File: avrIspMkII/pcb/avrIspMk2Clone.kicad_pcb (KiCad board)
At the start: 2 copper layers, 50 x 40 mm, 42 parts, among them IC1 ATMEGA8-16AU, J1 DB9, P1 USB_OTG, P2 CONN_01X03, P3 CONN_01X02, P4 CONN_02X05, P5 CONN_02X03, SW1 SW_SPDT, SW2 SW_SPDT, U1 LM1117-3.3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

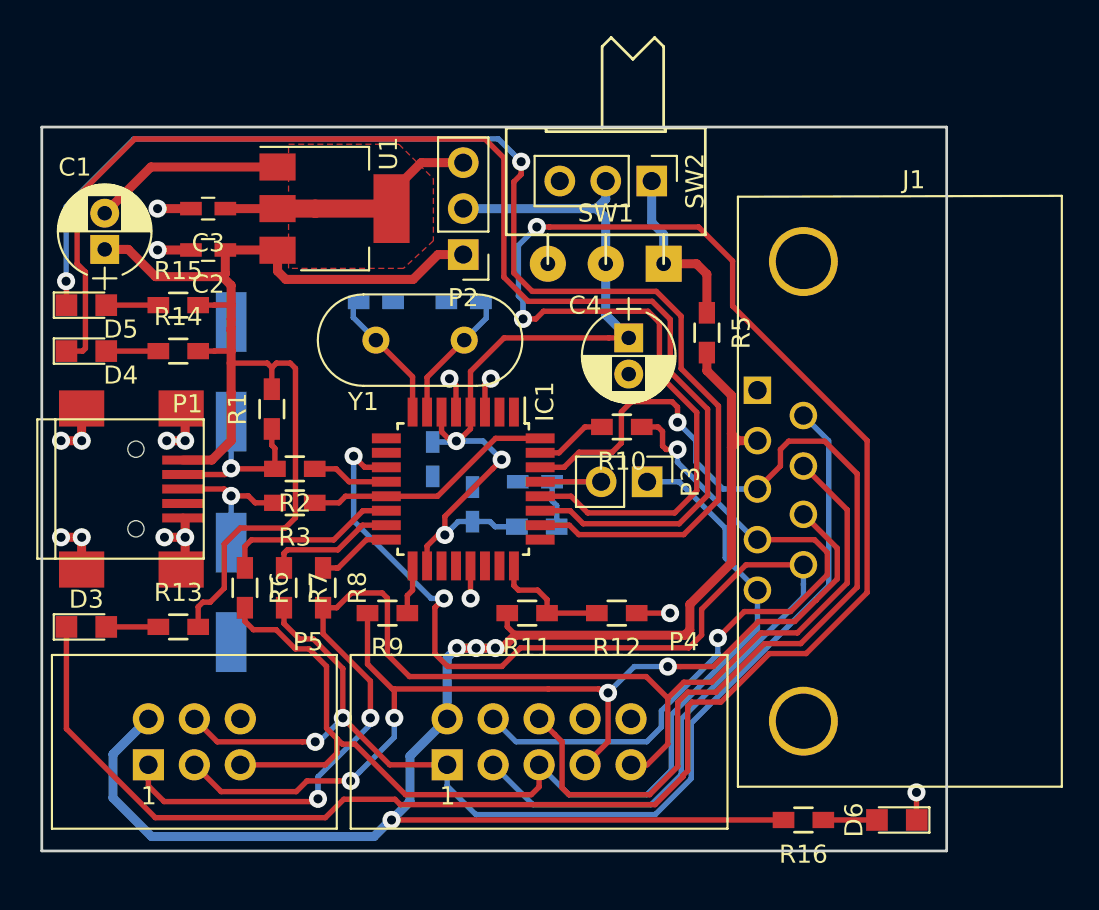
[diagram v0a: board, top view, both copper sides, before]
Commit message: finished layout for avrIspMk2Clone
generated documentation and gerber files
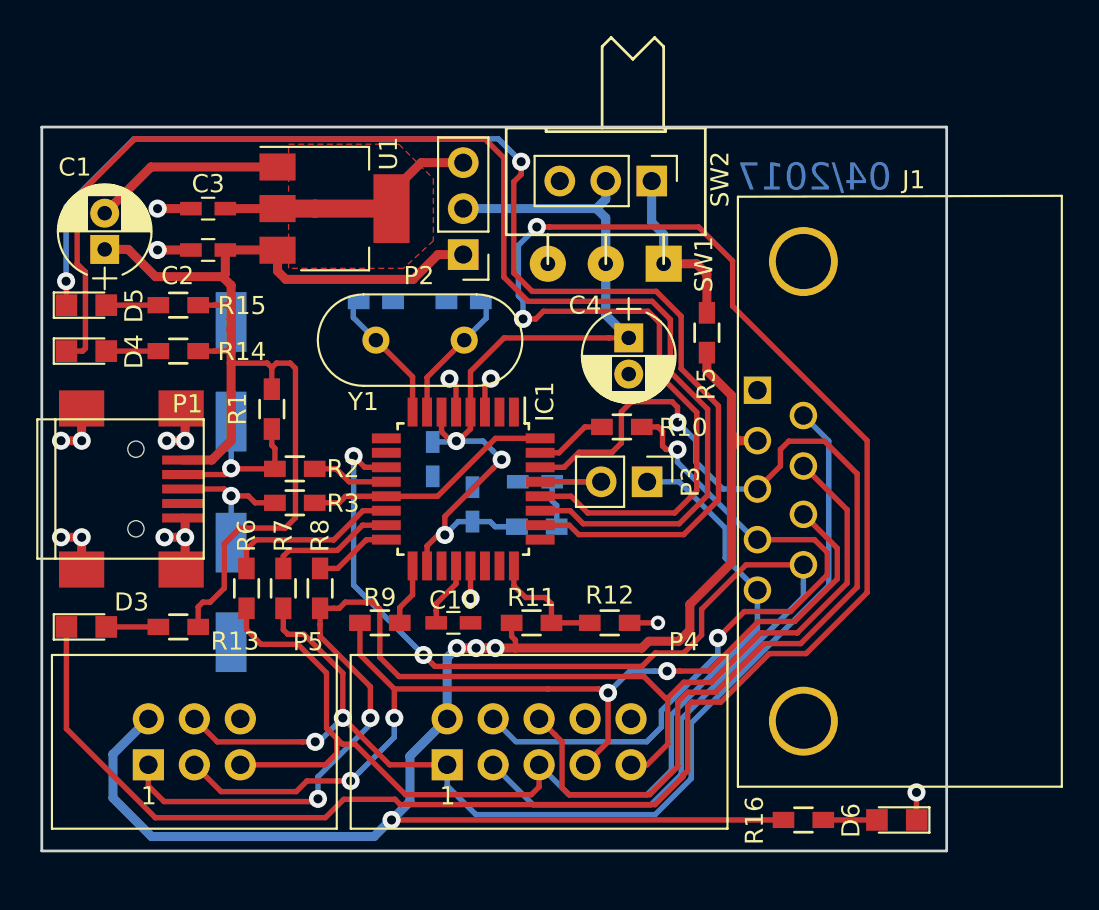
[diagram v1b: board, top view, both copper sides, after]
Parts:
- added C10: 100n, Capacitors_SMD:C_0603_HandSoldering, F.Cu at (102.7, 112.4)
- added G***: LOGO, proz_logo:Shimatta_SolderMask, B.Cu at (126.5, 105.0)
- added REF**: KiCAD Logo, Symbols:Symbol_KiCAD-Logo_CopperAndSilkScreenTop, B.Cu at (94.4, 89.4)
- added REF***: WEEE-Logo_4.2x6mm_SilkScreen, Symbols:WEEE-Logo_4.2x6mm_SilkScreen, B.Cu at (84.8, 112.1)
- moved R9 0.68 mm to (98.7, 112.4)
- moved R12 0.67 mm to (111.4, 112.4)
- moved R11 0.59 mm to (107.1, 112.4)
- moved R8 0.17 mm to (95.4, 110.5)
- moved R6 0.09 mm to (91.3, 110.5)
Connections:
- net /MEASSURE renamed /MEASURE
- IC1 pad 20: (no net) -> /AVREF
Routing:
- net /AVREF: track 0.00 -> 3.60 mm
- net Net-(IC1-Pad17): track 2.79 -> 3.44 mm
- net /MISO_OUT: track 72.6 -> 72.0 mm
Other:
- board text added: "04/2017"

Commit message: finished some layouts
added pcb numbering and revision
added a pcb list
orderes the pcbs
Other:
- board text added: "05/2017 Rev: 1.0 0001"
- board text removed: "04/2017"
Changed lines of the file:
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@@
-(kicad_pcb (version 20160815) (host pcbnew "(2017-01-09 revision c2fb336)-makepkg")
+(kicad_pcb (version 20170123) (host pcbnew "(2017-05-12 revision b823d0b78)-makepkg")
   (general
-    (links 0)
+    (links 102)
     (no_connects 0)
-    (area 79.924999 84.924999 130.075001 125.075001)
+    (area 71.380048 79.728999 145.469001 126.6055)
     (thickness 1.6)
     (drawings 5)
@@
   )
   (page A4)
+  (title_block
+    (title avrIspMk2Clone)
+    (date 2017-05-13)
+    (rev 1.0)
+    (company shimatta)
+  )
   (layers
     (0 F.Cu signal)
@@
     (visible_elements 7FFFFFFF)
     (pcbplotparams
-      (layerselection 0x010f0_ffffffff)
+      (layerselection 0x010fc_ffffffff)
       (usegerberextensions true)
-      (excludeedgelayer true)
+      (excludeedgelayer false)
       (linewidth 0.100000)
-      (plotframeref false)
+      (plotframeref true)
       (viasonmask false)
       (mode 1)
-      (useauxorigin true)
+      (useauxorigin false)
       (hpglpennumber 1)
       (hpglpenspeed 20)
@@
       (psa4output false)
       (plotreference true)
-      (plotvalue false)
+      (plotvalue true)
       (plotinvisibletext false)
       (padsonsilk false)
       (subtractmaskfromsilk false)
-      (outputformat 1)
+      (outputformat 4)
       (mirror false)
-      (drillshape 0)
+      (drillshape 2)
       (scaleselection 1)
-      (outputdirectory gerber/))
+      (outputdirectory doc/))
   )
   (net 0 "")
@@
     )
   )
-  (gr_text 04/2017 (at 122.682 87.757) (layer B.Cu)
-    (effects (font (size 1.5 1.5) (thickness 0.3)) (justify mirror))
+  (gr_text "05/2017\nRev: 1.0\n0001" (at 129.286 88.265) (layer B.Cu)
+    (effects (font (size 1 1) (thickness 0.2)) (justify left mirror))
   )
   (gr_line (start 130 85) (end 80 85) (layer Edge.Cuts) (width 0.15))
